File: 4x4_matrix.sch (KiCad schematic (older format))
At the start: 32 parts

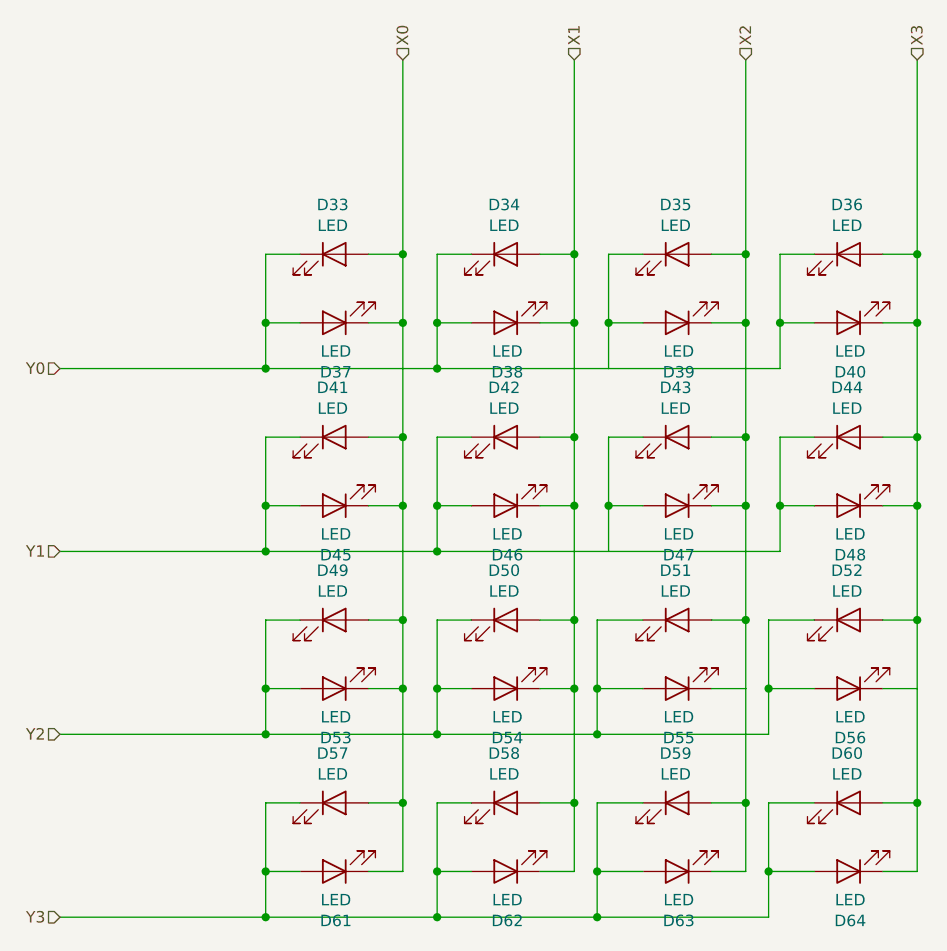
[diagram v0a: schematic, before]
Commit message: Reduce LEDs by half
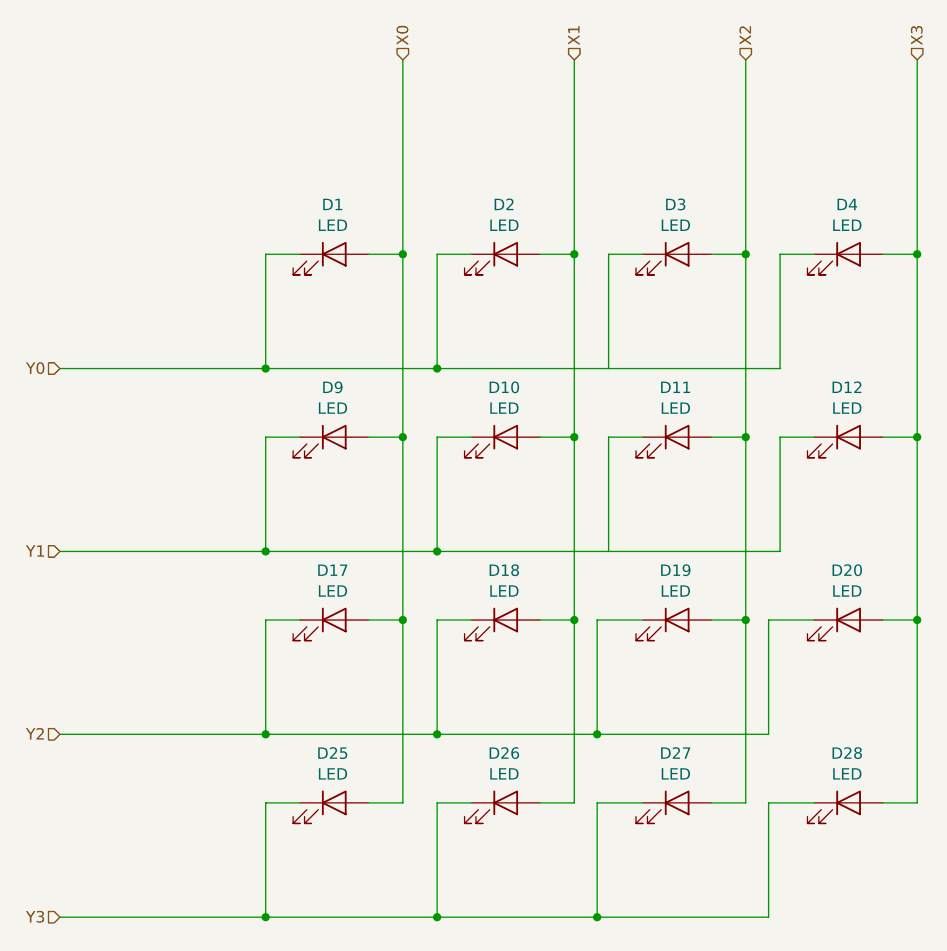
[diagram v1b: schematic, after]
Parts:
- removed D13, D14, D15, D16, D21, D22, D23, D24, D29, D30, D31, D32, D5, D6, D7, D8: LED, LED_SMD:LED_0805_2012Metric, symbol Device:LED
